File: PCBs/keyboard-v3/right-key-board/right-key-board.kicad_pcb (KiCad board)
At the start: 2 copper layers, 115 x 86 mm, 49 parts

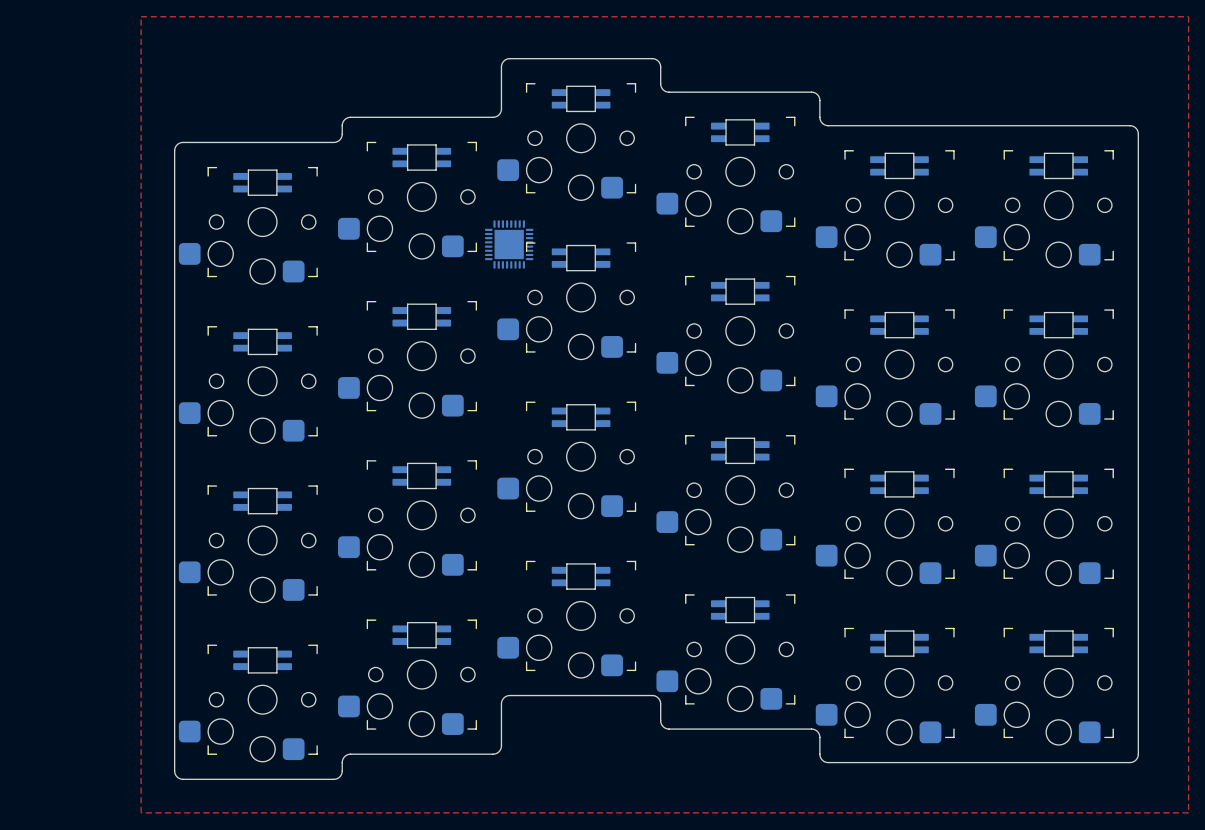
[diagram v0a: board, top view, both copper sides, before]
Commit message: Key board schematic done and layout half done
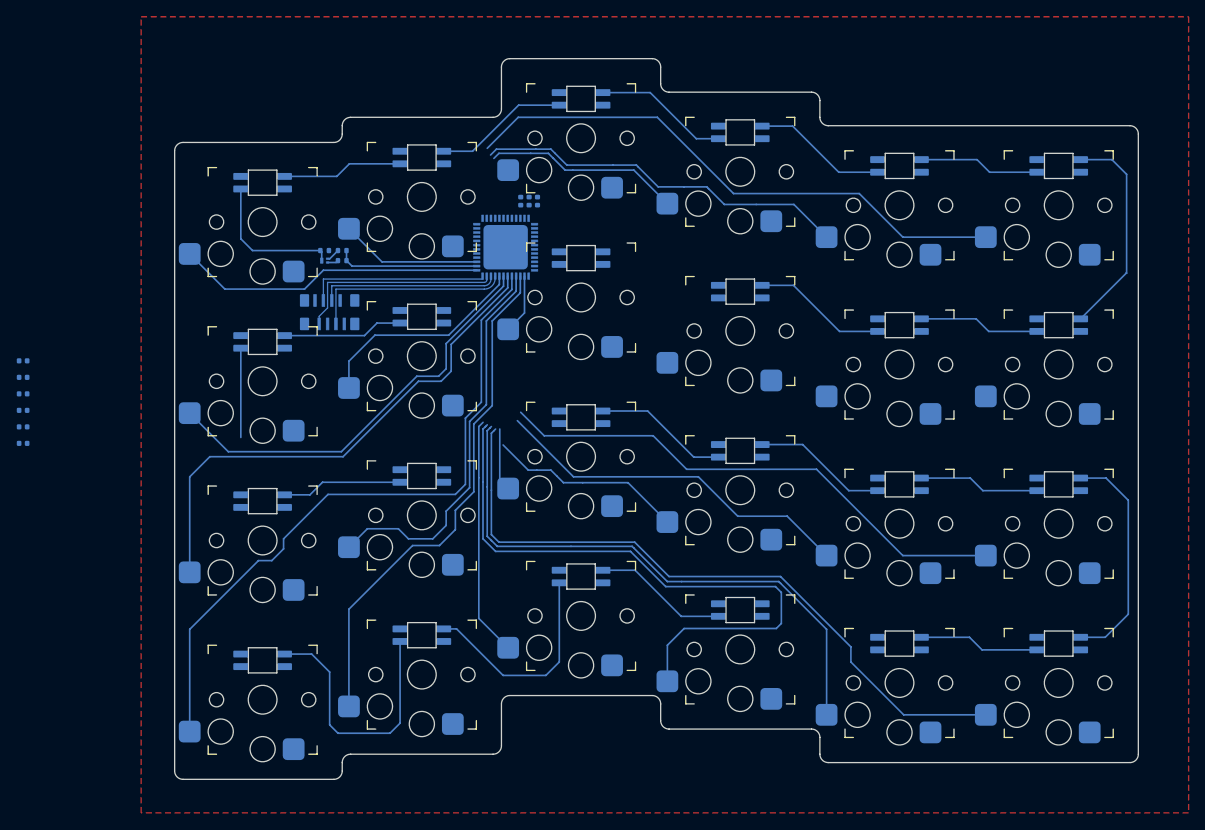
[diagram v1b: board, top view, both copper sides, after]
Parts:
- removed REF** (x24): SW_Kailh_Choc_V1_HotSwap, project_footprints:SW_Kailh_Choc_V1_HotSwap
- removed REF** (x24): ${REFERENCE}, project_footprints:sk6812-e
- removed REF**: UFQFPN-32-1EP_5x5mm_P0.5mm_EP3.5x3.5mm, Package_DFN_QFN:UFQFPN-32-1EP_5x5mm_P0.5mm_EP3.5x3.5mm
- added C201: 1u, project_footprints:C_0402, B.Cu at (75.9, 95.9)
- added C202: 1u, project_footprints:C_0402, B.Cu at (75.9, 93.9)
- added C203: 1u, project_footprints:C_0402, B.Cu at (75.9, 92.0)
- added C204: 1u, project_footprints:C_0402, B.Cu at (75.9, 90.0)
- added C205: 1u, project_footprints:C_0402, B.Cu at (75.9, 88.0)
- added C206: 1u, project_footprints:C_0402, B.Cu at (75.9, 86.1)
- added C301: 1u, project_footprints:C_0402, B.Cu at (137.3, 67.0)
- added C302: 100n, project_footprints:C_0402, B.Cu at (135.3, 67.0)
- added C303: 4u7, project_footprints:C_0402, B.Cu at (136.3, 67.0)
- added D201: SK6812-E, project_footprints:sk6812-e, B.Cu at (104.5, 64.8)
- added D202: SK6812-E, project_footprints:sk6812-e, B.Cu at (199.5, 81.8)
- added D203: SK6812-E, project_footprints:sk6812-e, B.Cu at (104.5, 102.8)
- added D204: SK6812-E, project_footprints:sk6812-e, B.Cu at (199.5, 119.8)
- added D205: SK6812-E, project_footprints:sk6812-e, B.Cu at (123.5, 61.8)
- added D206: SK6812-E, project_footprints:sk6812-e, B.Cu at (180.5, 81.8)
- added D207: SK6812-E, project_footprints:sk6812-e, B.Cu at (123.5, 99.8)
- added D208: SK6812-E, project_footprints:sk6812-e, B.Cu at (180.5, 119.8)
- added D209: SK6812-E, project_footprints:sk6812-e, B.Cu at (142.5, 54.8)
- added D210: SK6812-E, project_footprints:sk6812-e, B.Cu at (161.5, 77.8)
- added D211: SK6812-E, project_footprints:sk6812-e, B.Cu at (142.5, 92.8)
- added D212: SK6812-E, project_footprints:sk6812-e, B.Cu at (161.5, 115.8)
- added D213: SK6812-E, project_footprints:sk6812-e, B.Cu at (161.5, 58.8)
- added D214: SK6812-E, project_footprints:sk6812-e, B.Cu at (142.5, 73.8)
- added D215: SK6812-E, project_footprints:sk6812-e, B.Cu at (161.5, 96.8)
- added D216: SK6812-E, project_footprints:sk6812-e, B.Cu at (142.5, 111.8)
- added D217: SK6812-E, project_footprints:sk6812-e, B.Cu at (180.5, 62.8)
- added D218: SK6812-E, project_footprints:sk6812-e, B.Cu at (123.5, 80.8)
- added D219: SK6812-E, project_footprints:sk6812-e, B.Cu at (180.5, 100.8)
- added D220: SK6812-E, project_footprints:sk6812-e, B.Cu at (123.5, 118.8)
- added D221: SK6812-E, project_footprints:sk6812-e, B.Cu at (199.5, 62.8)
- added D222: SK6812-E, project_footprints:sk6812-e, B.Cu at (104.5, 83.8)
- added D223: SK6812-E, project_footprints:sk6812-e, B.Cu at (199.5, 100.8)
- added D224: SK6812-E, project_footprints:sk6812-e, B.Cu at (104.5, 121.8)
- added J301: F31Z1A7H111008, project_footprints:F31Z1A7H111008, B.Cu at (112.5, 80.0)
- added Q201: DMN21D2UFB-7B, project_footprints:DMN21D2UFB7B, B.Cu at (111.9, 74.1)
- added R201: 10k, project_footprints:R_0402, B.Cu at (114.0, 74.1)
- added R202: 2k2, project_footprints:R_0402, B.Cu at (114.0, 72.9)
- added R203: 2k2, project_footprints:R_0402, B.Cu at (111.9, 72.9)
- added SW201: SW_DIP_x01, project_footprints:SW_Kailh_Choc_V1_HotSwap, F.Cu at (104.5, 69.5)
- added SW202: SW_DIP_x01, project_footprints:SW_Kailh_Choc_V1_HotSwap, F.Cu at (104.5, 88.5)
- added SW203: SW_DIP_x01, project_footprints:SW_Kailh_Choc_V1_HotSwap, F.Cu at (104.5, 107.5)
- added SW204: SW_DIP_x01, project_footprints:SW_Kailh_Choc_V1_HotSwap, F.Cu at (104.5, 126.5)
- added SW205: SW_DIP_x01, project_footprints:SW_Kailh_Choc_V1_HotSwap, F.Cu at (123.5, 66.5)
- added SW206: SW_DIP_x01, project_footprints:SW_Kailh_Choc_V1_HotSwap, F.Cu at (123.5, 85.5)
- added SW207: SW_DIP_x01, project_footprints:SW_Kailh_Choc_V1_HotSwap, F.Cu at (123.5, 104.5)
- added SW208: SW_DIP_x01, project_footprints:SW_Kailh_Choc_V1_HotSwap, F.Cu at (123.5, 123.5)
- added SW209: SW_DIP_x01, project_footprints:SW_Kailh_Choc_V1_HotSwap, F.Cu at (142.5, 59.5)
- added SW210: SW_DIP_x01, project_footprints:SW_Kailh_Choc_V1_HotSwap, F.Cu at (142.5, 78.5)
- added SW211: SW_DIP_x01, project_footprints:SW_Kailh_Choc_V1_HotSwap, F.Cu at (142.5, 97.5)
- added SW212: SW_DIP_x01, project_footprints:SW_Kailh_Choc_V1_HotSwap, F.Cu at (142.5, 116.5)
- added SW213: SW_DIP_x01, project_footprints:SW_Kailh_Choc_V1_HotSwap, F.Cu at (161.5, 63.5)
- added SW214: SW_DIP_x01, project_footprints:SW_Kailh_Choc_V1_HotSwap, F.Cu at (161.5, 82.5)
- added SW215: SW_DIP_x01, project_footprints:SW_Kailh_Choc_V1_HotSwap, F.Cu at (161.5, 101.5)
- added SW216: SW_DIP_x01, project_footprints:SW_Kailh_Choc_V1_HotSwap, F.Cu at (161.5, 120.5)
- added SW217: SW_DIP_x01, project_footprints:SW_Kailh_Choc_V1_HotSwap, F.Cu at (180.5, 67.5)
- added SW218: SW_DIP_x01, project_footprints:SW_Kailh_Choc_V1_HotSwap, F.Cu at (180.5, 86.5)
- added SW219: SW_DIP_x01, project_footprints:SW_Kailh_Choc_V1_HotSwap, F.Cu at (180.5, 105.5)
- added SW220: SW_DIP_x01, project_footprints:SW_Kailh_Choc_V1_HotSwap, F.Cu at (180.5, 124.5)
- added SW221: SW_DIP_x01, project_footprints:SW_Kailh_Choc_V1_HotSwap, F.Cu at (199.5, 67.5)
- added SW222: SW_DIP_x01, project_footprints:SW_Kailh_Choc_V1_HotSwap, F.Cu at (199.5, 86.5)
- added SW223: SW_DIP_x01, project_footprints:SW_Kailh_Choc_V1_HotSwap, F.Cu at (199.5, 105.5)
- added SW224: SW_DIP_x01, project_footprints:SW_Kailh_Choc_V1_HotSwap, F.Cu at (199.5, 124.5)
- added U301: STM32G0C1CEUx, project_footprints:QFN50P700X700X60-49N-D, B.Cu at (133.5, 72.5)
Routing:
- net /Keys/KEY_L4: track 0.00 -> 81.8 mm
- net /Keys/KEY_G4: track 0.00 -> 80.1 mm
- net /Keys/KEY_J4: track 0.00 -> 74.7 mm
- net /Keys/KEY_K4: track 0.00 -> 68.6 mm
- net /Keys/KEY_L1: track 0.00 -> 67.0 mm
- net /Keys/KEY_L3: track 0.00 -> 62.6 mm
- net /Keys/KEY_G3: track 0.00 -> 62.0 mm
- net /Keys/KEY_H4: track 0.00 -> 61.7 mm
- net /Keys/KEY_G2: track 0.00 -> 50.5 mm
- net /Keys/KEY_H3: track 0.00 -> 46.9 mm
- net /Keys/KEY_K1: track 0.00 -> 44.7 mm
- net /Keys/KEY_K3: track 0.00 -> 43.6 mm
- net /Keys/KEY_G1: track 0.00 -> 36.9 mm
- net /Keys/LED24: track 0.00 -> 31.7 mm
- net /Keys/KEY_I4: track 0.00 -> 28.6 mm
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
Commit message: Right daughter boards finished
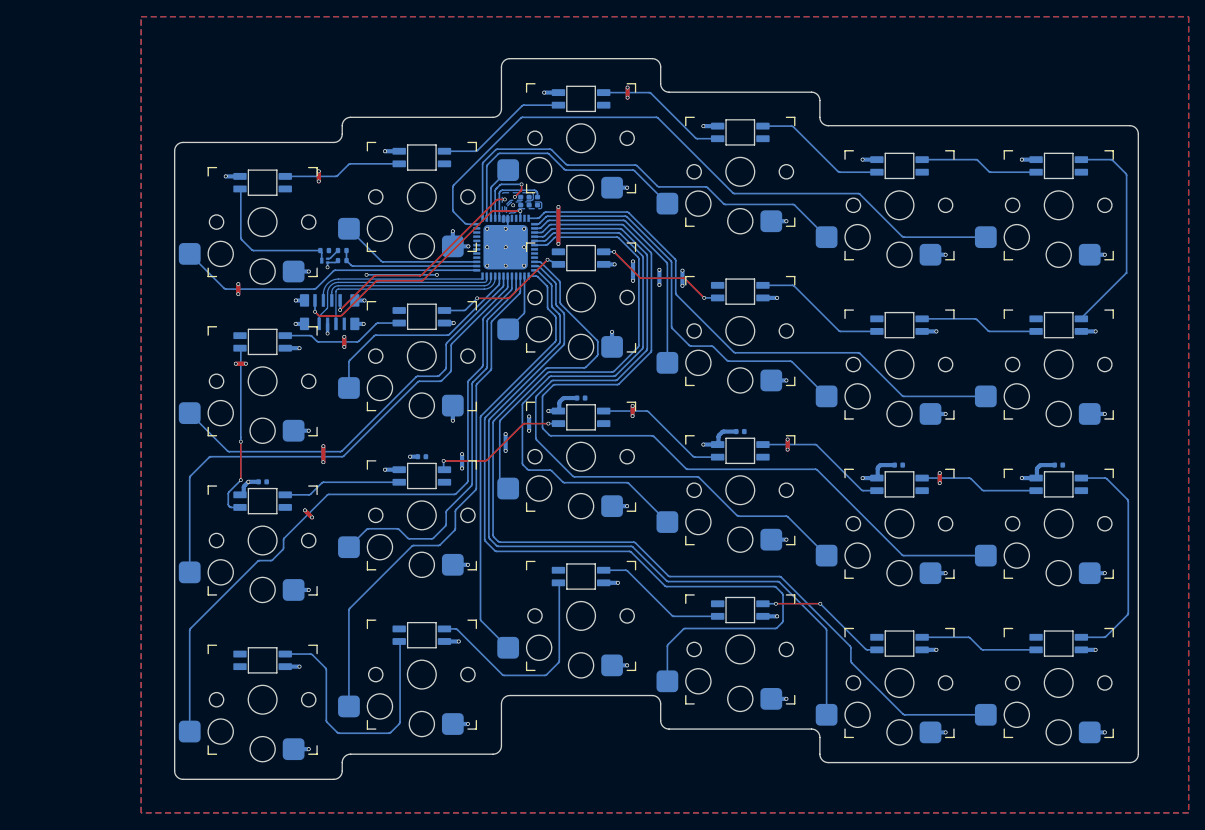
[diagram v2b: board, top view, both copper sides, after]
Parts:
- moved C202 123.7 mm to (199.5, 98.5), turned to 180 degrees
- moved C203 104.7 mm to (180.4, 98.5), turned to 180 degrees
- moved C204 85.7 mm to (161.5, 94.5), turned to 180 degrees
- moved C205 66.6 mm to (142.5, 90.5), turned to 180 degrees
- moved C206 48.9 mm to (123.5, 97.5), turned to 180 degrees
- moved C201 28.9 mm to (104.5, 100.5), turned to 180 degrees
- moved J301 0.25 mm to (112.5, 80.2)
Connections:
- net VBUS renamed +5V
- U301 pad 1: unconnected-(U301-PC13-Pad1) -> /Keys/KEY_K1
- U301 pad 12: unconnected-(U301-PA1-Pad12) -> /Keys/KEY_L2
- U301 pad 13: unconnected-(U301-PA2-Pad13) -> /Keys/KEY_K2
- U301 pad 14: unconnected-(U301-PA3-Pad14) -> /Keys/KEY_J2
- U301 pad 15: unconnected-(U301-PA4-Pad15) -> /Keys/KEY_L3
- U301 pad 16: unconnected-(U301-PA5-Pad16) -> /Keys/KEY_K3
- U301 pad 17: unconnected-(U301-PA6-Pad17) -> /Keys/KEY_J3
- U301 pad 18: unconnected-(U301-PA7-Pad18) -> /Keys/KEY_I3
- U301 pad 2: unconnected-(U301-PC14-Pad2) -> /Keys/KEY_J1
- U301 pad 22: unconnected-(U301-PB10-Pad22) -> /Keys/KEY_L4
- U301 pad 23: unconnected-(U301-PB11-Pad23) -> /Keys/KEY_K4
- U301 pad 24: unconnected-(U301-PB12-Pad24) -> /Keys/KEY_J4
- U301 pad 25: unconnected-(U301-PB13-Pad25) -> /Keys/KEY_I4
- U301 pad 3: unconnected-(U301-PC15-Pad3) -> /Keys/KEY_I1
- U301 pad 48: unconnected-(U301-PB9-Pad48) -> /Keys/KEY_L1
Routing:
- net GND: track 1.33 -> 132.3 mm, vias 0 -> 80
- net /Keys/KEY_L2: track 0.00 -> 66.3 mm
- net /Keys/KEY_K2: track 0.00 -> 48.6 mm
- net /Keys/KEY_J3: track 23.4 -> 69.8 mm
- net /Keys/KEY_I3: track 7.51 -> 53.1 mm
- net /Keys/KEY_K3: track 43.6 -> 87.4 mm
- net /Keys/KEY_L3: track 62.6 -> 105.5 mm
- net +3V3: track 0.00 -> 34.8 mm, vias 0 -> 4
- net /MCU/~{RST}: track 0.00 -> 32.0 mm, vias 0 -> 2
- net /Keys/KEY_L4: track 81.8 -> 112.6 mm
- net /Keys/KEY_J2: track 0.00 -> 30.2 mm
- net /Keys/KEY_K4: track 68.6 -> 92.8 mm
- net /Keys/KEY_J4: track 74.7 -> 98.0 mm
- net /Keys/KEY_I4: track 28.6 -> 51.3 mm
- net +5V: track 0.00 -> 17.1 mm, vias 0 -> 22
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- added copper zone on B.Cu, net +3V3
- added copper zone on B.Cu, net +5V
- added copper zone on B.Cu, net GND
- added copper zone on F.Cu, net GND
- removed copper zone on F.Cu, net (none)

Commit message: Added debug-breakout board, progress on right side schematics & layout
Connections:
- J301 pad 7: /MCU/SWDIO -> /MCU/SWDIO/~{INT}
- U301 pad 35: /MCU/SWDIO -> /MCU/SWDIO/~{INT}
- U301 pad 37: /Keys/KEY_G1 -> /MCU/SWDIO/~{INT}
- U301 pad 38: /Keys/NEOPIXEL -> /Keys/KEY_G1
- U301 pad 39: /Keys/KEY_H1 -> /Keys/NEOPIXEL
- U301 pad 40: unconnected-(U301-PD2-Pad40) -> /Keys/KEY_H1
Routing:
- net /MCU/SWDIO/~{INT}: track 0.00 -> 26.5 mm, vias 0 -> 2
- net /MCU/SWDIO: track 24.3 -> 0.00 mm
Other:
- board text added: "'"
- board text added: ","
- board text added: "."
- board text added: "/"
- board text added: "0"
- board text added: "6"
- board text added: "7"
- board text added: "8"
- board text added: "9"
- board text added: ";"
- board text added: "="
- board text added: "H"
- board text added: "I"
- board text added: "J"
- board text added: "K"
- board text added: "L"
- board text added: "M"
- board text added: "N"
- board text added: "O"
- board text added: "P"
- board text added: "U"
- board text added: "Y"
- board text added: "["
- board text added: "]"

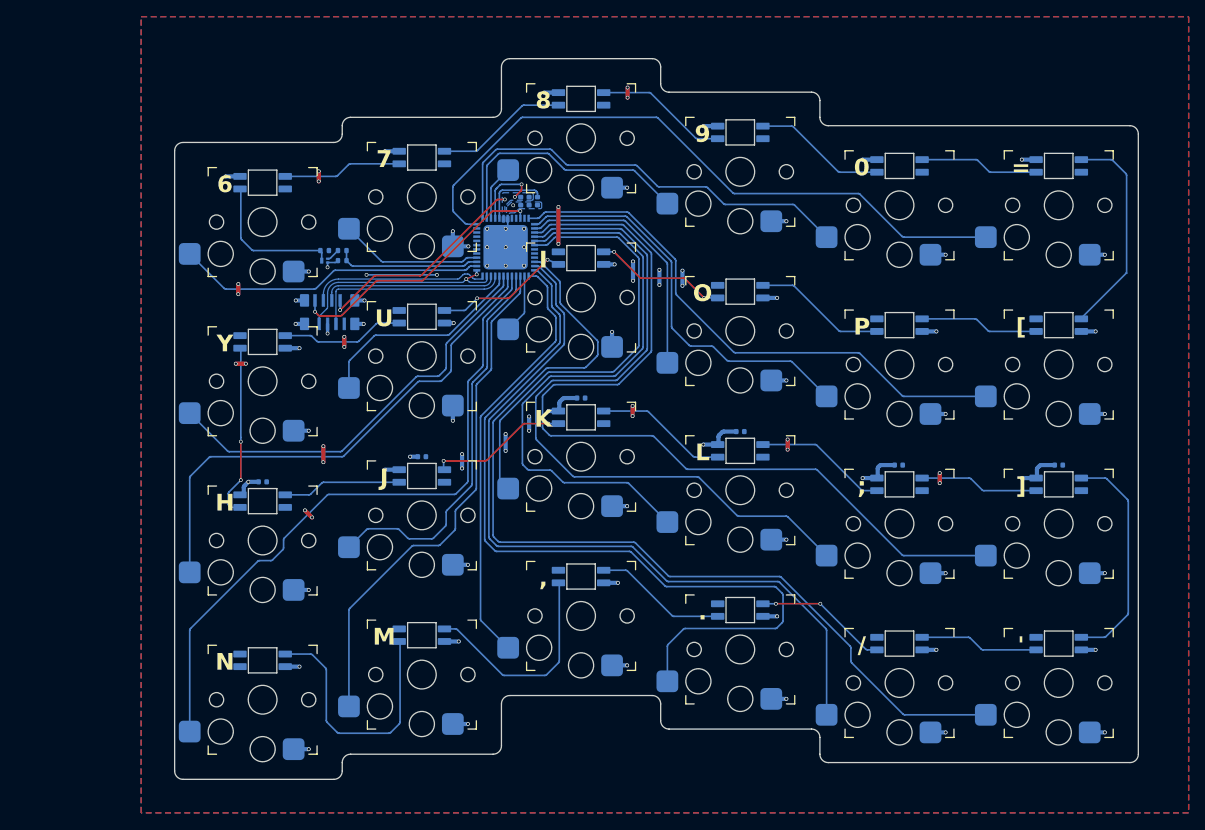
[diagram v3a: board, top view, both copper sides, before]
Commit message: Right control board placement and schematic done
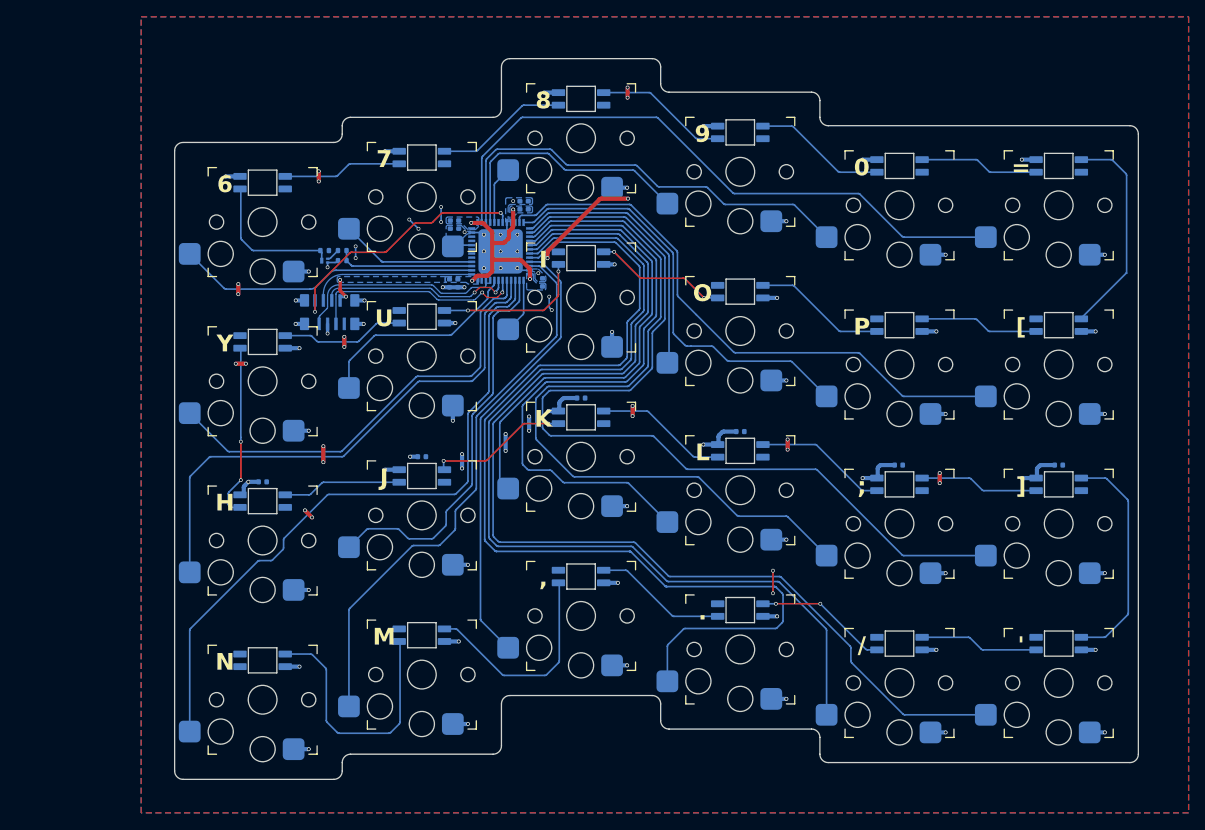
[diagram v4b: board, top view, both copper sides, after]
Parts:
- removed C301: 1u, project_footprints:C_0402
- removed C302: 100n, project_footprints:C_0402
- removed C303: 4u7, project_footprints:C_0402
- removed U301: STM32G0C1CEUx, project_footprints:QFN50P700X700X60-49N-D
- added C1: 1u, project_footprints:C_0402, B.Cu at (136.2, 67.5)
- added C105: 4u7, project_footprints:C_0402, B.Cu at (127.9, 69.8)
- added C106: 100n, project_footprints:C_0402, B.Cu at (137.9, 76.7)
- added C107: 100n, project_footprints:C_0402, B.Cu at (126.9, 69.8)
- added C108: 100n, project_footprints:C_0402, B.Cu at (135.2, 67.5)
- added C2: 100n, project_footprints:C_0402, B.Cu at (127.8, 76.8)
- added C3: 4u7, project_footprints:C_0402, B.Cu at (126.8, 76.8)
- added U302: STM32U031C6Ux, project_footprints:QFN50P700X700X60-49N-D, B.Cu at (132.9, 73.0)
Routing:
- net /Keys/KEY_J4: track 98.0 -> 121.7 mm
- net /Keys/KEY_K4: track 92.8 -> 116.4 mm
- net /Keys/KEY_L4: track 112.6 -> 130.7 mm
- net +5V: track 17.1 -> 28.4 mm, vias 22 -> 24
- net +3V3: track 34.8 -> 25.3 mm, vias 4 -> 6
- net /MCU/VREF+: track 8.37 -> 0.00 mm
- net GND: track 132.3 -> 139.3 mm, vias 80 -> 82
- net /Keys/KEY_H4: track 61.6 -> 66.6 mm
- net /Keys/KEY_L3: track 105.5 -> 110.1 mm
- net /Keys/KEY_K3: track 87.4 -> 91.9 mm
- net /Keys/KEY_I3: track 53.1 -> 57.5 mm
- net /Keys/KEY_J3: track 69.8 -> 74.2 mm
- net /Keys/KEY_L1: track 79.3 -> 75.8 mm
- net /Keys/KEY_L2: track 66.3 -> 69.4 mm
- net /Keys/KEY_K2: track 48.6 -> 51.6 mm
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
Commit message: Added mounting holes
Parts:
- added H101: MountingHole, MountingHole:MountingHole_2.2mm_M2, F.Cu at (190.0, 115.0)
- added H102: MountingHole, MountingHole:MountingHole_2.2mm_M2, F.Cu at (190.0, 77.0)
- added H103: MountingHole, MountingHole:MountingHole_2.2mm_M2, F.Cu at (114.0, 63.0)
- added H104: MountingHole, MountingHole:MountingHole_2.2mm_M2, F.Cu at (114.0, 117.0)
- renumbered C108 to C301, C1 to C302, C2 to C303, C106 to C304, C107 to C305, C3 to C306, C105 to C307, D205 to D202, D209 to D203, D213 to D204, D217 to D205, D221 to D206, D202 to D207, D206 to D208, D210 to D209, D214 to D210, D218 to D211, D222 to D212, D203 to D213, D207 to D214, D211 to D215, D215 to D216, D219 to D217, D223 to D218, D204 to D219, D208 to D220, D212 to D221, D216 to D222, D220 to D223, R203 to R201, R201 to R203, SW205 to SW202, SW209 to SW203, SW213 to SW204, SW217 to SW205, SW221 to SW206, SW202 to SW207, SW206 to SW208, SW210 to SW209, SW214 to SW210, SW218 to SW211, SW222 to SW212, SW203 to SW213, SW207 to SW214, SW211 to SW215, SW215 to SW216, SW219 to SW217, SW223 to SW218, SW204 to SW219, SW208 to SW220, SW212 to SW221, SW216 to SW222, SW220 to SW223, U302 to U301
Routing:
- net /Keys/LED2: track 14.4 -> 15.7 mm
- net +5V: track 28.4 -> 29.6 mm, vias 24 -> 26
